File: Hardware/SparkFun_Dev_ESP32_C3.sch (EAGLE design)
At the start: 36 parts, among them J1 USB Female Type C Connector, J4 QWIIC_RIGHT_ANGLE, U1 ESP32-C3, U2 RT9080-33GJ5, Y1 40MHZ

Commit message: Adds JTAG header and corrects boot control configuration
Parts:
- added FD1, FD2, FD3, FD4: FIDUCIALUFIDUCIAL, SparkFun-Aesthetics:FIDUCIALUFIDUCIAL
- added LOGO2: QWIIC_LOGO_3MM, SparkFun-Aesthetics:QWIIC_LOGO_3MM
- added LOGO3: OSHW-LOGOS, SparkFun-Aesthetics:OSHW-LOGOS
- added R7, R9: 100k, SparkFun-Resistors:100KOHM-0402T-1/16W-1%
- added TP1, TP2, TP3, TP4, TP5, TP6: TEST-POINT3X5, SparkFun-Connectors:TEST-POINT3X5
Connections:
- removed net IO20/TX: J5.12, U1.RXD/IO20
- removed net IO21/RX: J5.11, U1.TXD/IO21
- removed net IO4/A4: U1.MTMS/FSPIHD/IO4
- removed net IO5/A5: J6.6, U1.MTDI/FSPIWP/IO5
- removed net IO6/SCLK: J6.9, U1.MTCK/FSPICLK/IO6
- removed net IO7/PICO: J6.11, U1.MTDO/FSPID/IO7
- removed net IO8/BOOT: BOOT.2, C6.1, U1.IO8
- new net IO20/TXO: U1.RXD/IO20
- new net IO21/RXI: U1.TXD/IO21
- new net IO4/A4/MTMS: J6.5, TP4.1, U1.MTMS/FSPIHD/IO4
- new net IO5/A5/MTDI: TP6.1, U1.MTDI/FSPIWP/IO5
- new net IO6/SCLK/MTCK: J6.9, TP3.1, U1.MTCK/FSPICLK/IO6
- new net IO7/PICO/MTDO: J6.11, TP1.1, U1.MTDO/FSPID/IO7
- new net IO8: R7.1, U1.IO8
- new net IO9/BOOT: BOOT.2, C6.1, U1.IO9
- new net NC: J5.10, J5.9
- net 3.3V: now also R7.2, R9.2
- net EN: now also TP5.1
- net GND: now also J5.3, J5.4, TP2.1; no longer J5.10, J5.9
- net IO10: no longer J5.8
- net IO12: no longer J5.7
- net IO13/SDA: no longer J5.2
- net IO14/SCL: no longer J5.1
- net IO15: no longer J5.6
- net IO16: no longer J5.5
- net IO2/POCI: now also R9.1
- net IO3/A3: now also J6.6; no longer J6.5
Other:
- note added: "Cut PWR or STAT jumper to remove Power or Stat LEDs"
- note added: "JTAG Header"
- note removed: "Cut PWR jumper to remove power LED"
- moved on the sheet: J4, J5, J6

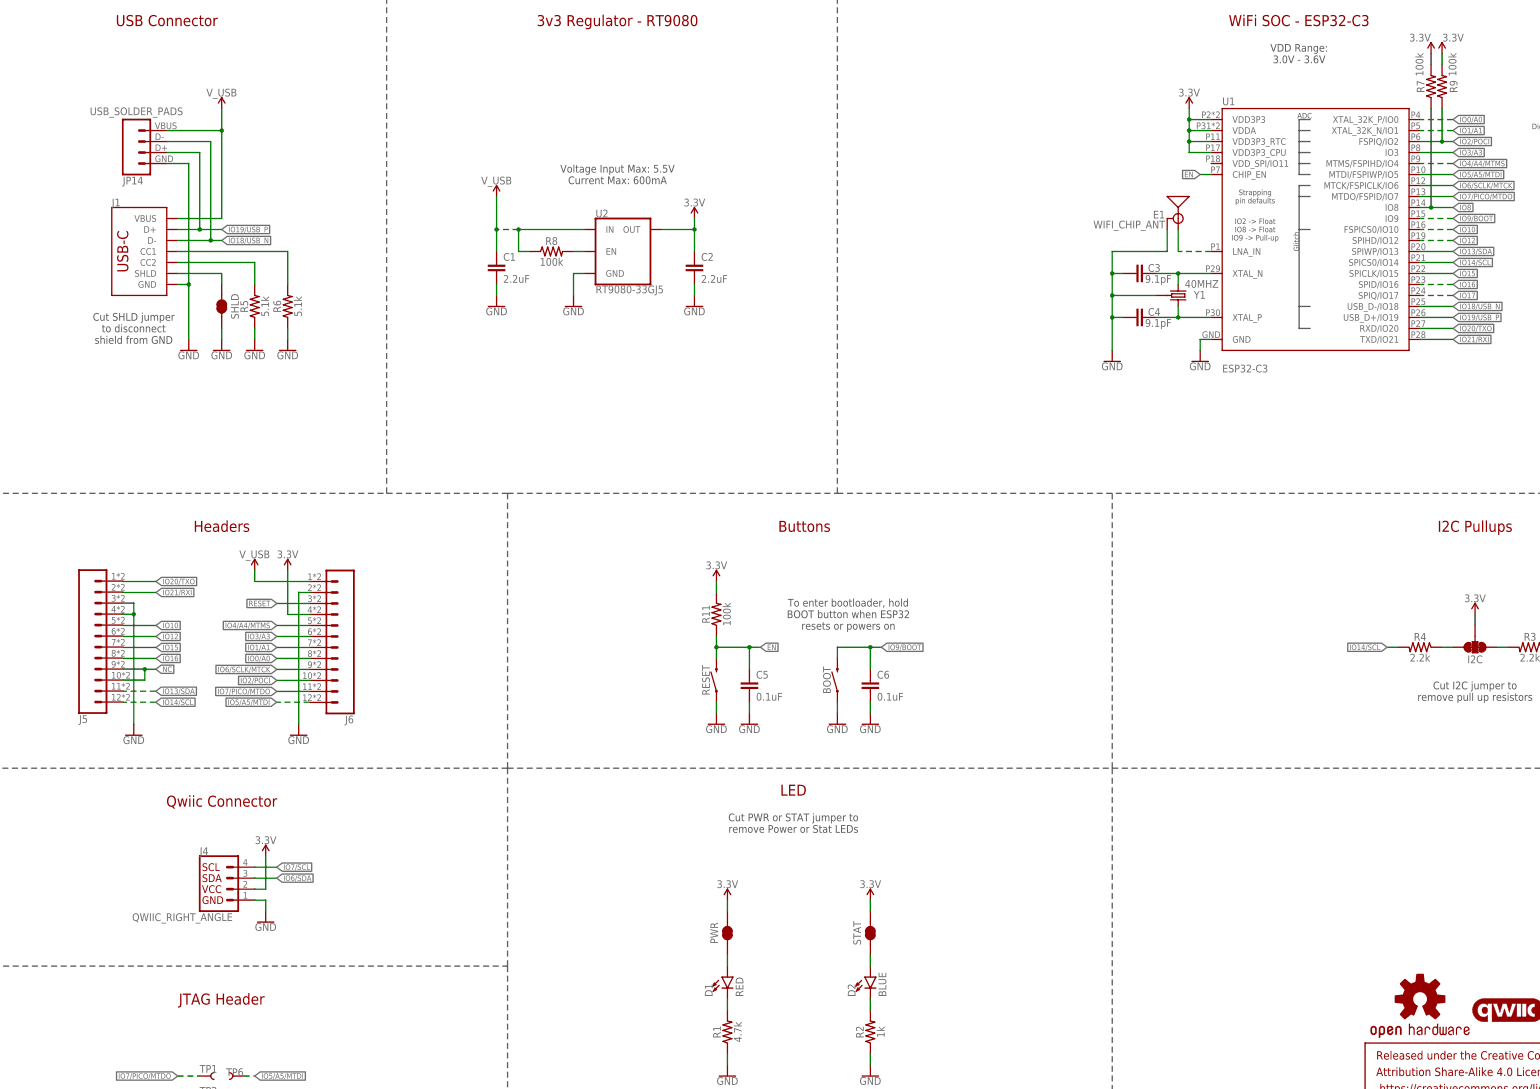
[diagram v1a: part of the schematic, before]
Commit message: Moves any connections away from antenna
* Finishes netting
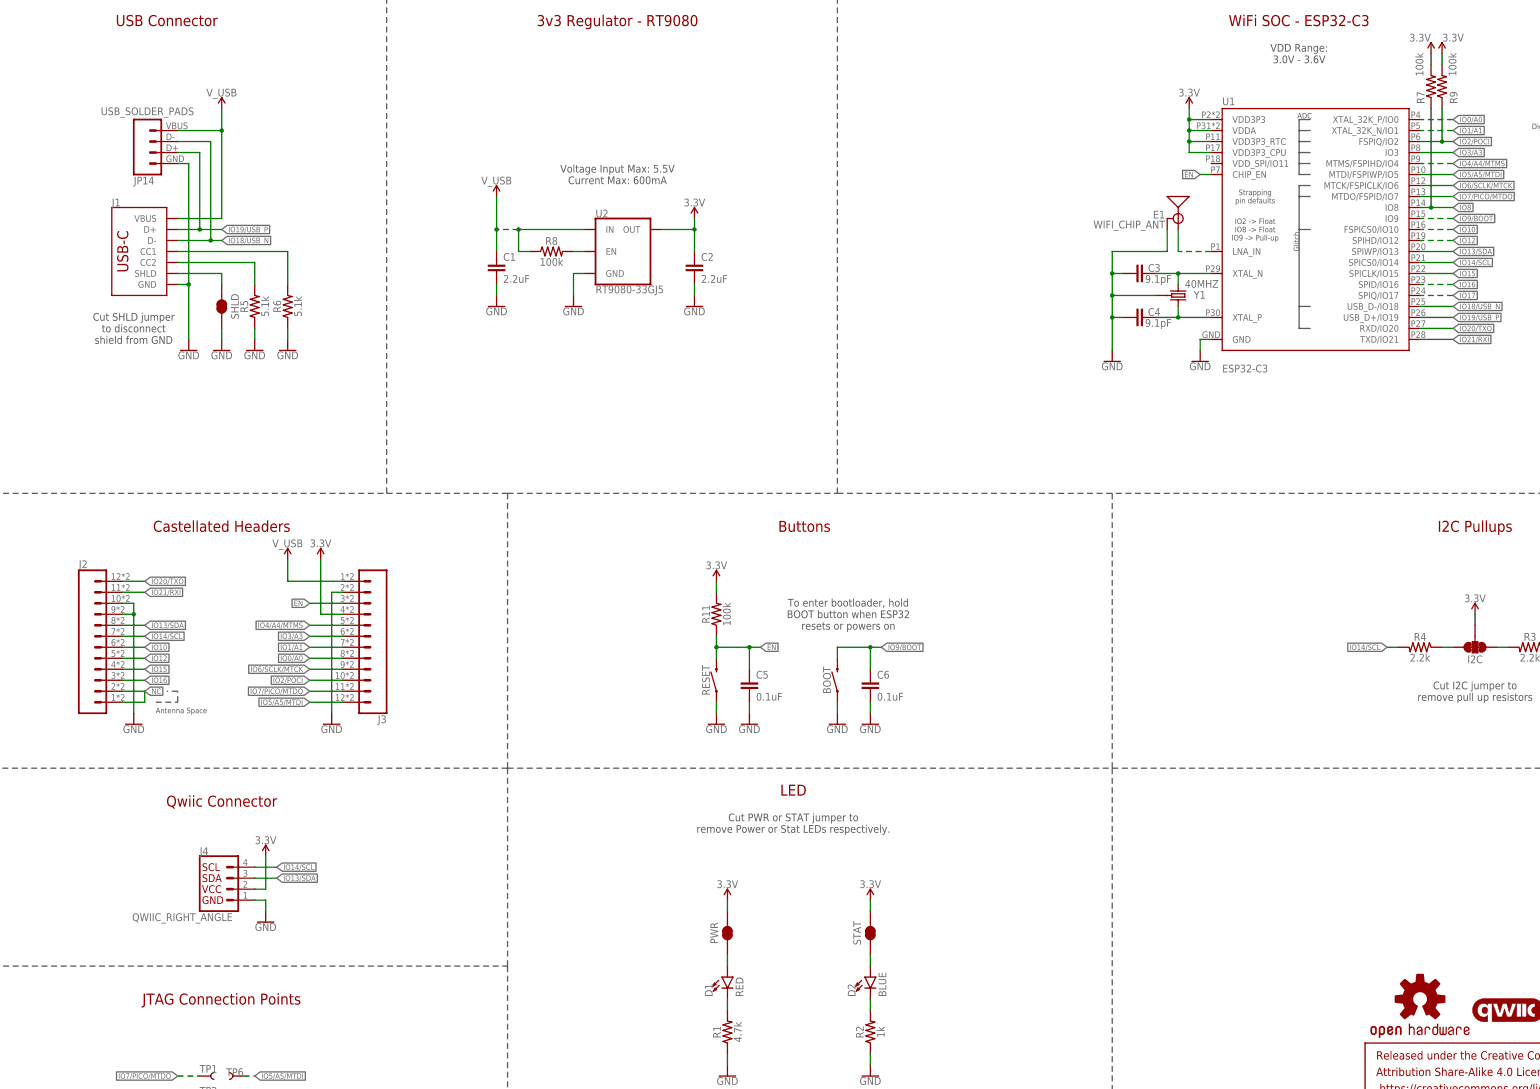
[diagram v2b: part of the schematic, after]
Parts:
- removed J5, J6: (no value), Castellated:CONN_12CASTLE
- added J2, J3: (no value), SparkFun-Connectors:CONN_12CASTELLATED
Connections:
- removed net !RESET!: J6.3
- removed net IO6/SDA: J4.3
- removed net IO7/SCL: J4.4
- removed net RAW: J6.1
- net 3.3V: now also J3.4; no longer J6.4
- net EN: now also J3.3
- net GND: now also J2.10, J2.9, J3.2; no longer J5.3, J5.4, J6.2
- net IO0/A0: now also J3.8; no longer J6.8
- net IO1/A1: now also J3.7; no longer J6.7
- net IO10: now also J2.6
- net IO12: now also J2.5
- net IO13/SDA: now also J2.8, J4.3
- net IO14/SCL: now also J2.7, J4.4
- net IO15: now also J2.4
- net IO16: now also J2.3
- net IO2/POCI: now also J3.10; no longer J6.10
- net IO20/TXO: now also J2.12
- net IO21/RXI: now also J2.11
- net IO3/A3: now also J3.6; no longer J6.6
- net IO4/A4/MTMS: now also J3.5; no longer J6.5
- net IO5/A5/MTDI: now also J3.12
- net IO6/SCLK/MTCK: now also J3.9; no longer J6.9
- net IO7/PICO/MTDO: now also J3.11; no longer J6.11
- net NC: now also J2.1, J2.2; no longer J5.10, J5.9
- net V_USB: now also J3.1
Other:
- note added: "Antenna Space"
- note added: "Castellated Headers"
- note added: "Cut PWR or STAT jumper to remove Power or Stat LEDs respectively."
- note added: "JTAG Connection Points"
- note removed: "Cut PWR or STAT jumper to remove Power or Stat LEDs"
- note removed: "Headers"
- note removed: "JTAG Header"
- moved on the sheet: JP14
